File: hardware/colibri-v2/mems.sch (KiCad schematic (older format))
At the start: 9 parts

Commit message: Annotated Components
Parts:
- gave numbers to parts that had none: 9
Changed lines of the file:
@@
 $EndDescr
 $Comp
-L L3GD20 U?
+L L3GD20 U2
 U 1 1 55865E51
 P 4800 3350
-F 0 "U?" H 5200 3850 60  0000 C CNN
+F 0 "U2" H 5200 3850 60  0000 C CNN
 F 1 "L3GD20" H 4500 2850 60  0000 C CNN
 F 2 "" H 4800 3500 60  0000 C CNN
@@
 $EndComp
 $Comp
-L C C?
+L C C36
 U 1 1 55865EFE
 P 6100 3450
-F 0 "C?" H 6125 3550 50  0000 L CNN
+F 0 "C36" H 6125 3550 50  0000 L CNN
 F 1 "10nF/25V" H 6125 3350 50  0000 L CNN
 F 2 "" H 6138 3300 30  0000 C CNN
@@
 $EndComp
 $Comp
-L C C?
+L C C38
 U 1 1 55865F5E
 P 6750 3200
-F 0 "C?" H 6775 3300 50  0000 L CNN
+F 0 "C38" H 6775 3300 50  0000 L CNN
 F 1 "10nF" H 6775 3100 50  0000 L CNN
 F 2 "" H 6788 3050 30  0000 C CNN
@@
 $EndComp
 $Comp
-L C C?
+L C C40
 U 1 1 55865F9A
 P 7350 3200
-F 0 "C?" H 7375 3300 50  0000 L CNN
+F 0 "C40" H 7375 3300 50  0000 L CNN
 F 1 "10uF" H 7375 3100 50  0000 L CNN
 F 2 "" H 7388 3050 30  0000 C CNN
@@
 $EndComp
 $Comp
-L GND #PWR?
+L GND #PWR40
 U 1 1 55865FDB
 P 6750 3950
-F 0 "#PWR?" H 6750 3700 50  0001 C CNN
+F 0 "#PWR40" H 6750 3700 50  0001 C CNN
 F 1 "GND" H 6750 3800 50  0000 C CNN
 F 2 "" H 6750 3950 60  0000 C CNN
@@
 $EndComp
 $Comp
-L GND #PWR?
+L GND #PWR39
 U 1 1 558661BB
 P 3950 3950
-F 0 "#PWR?" H 3950 3700 50  0001 C CNN
+F 0 "#PWR39" H 3950 3700 50  0001 C CNN
 F 1 "GND" H 3950 3800 50  0000 C CNN
 F 2 "" H 3950 3950 60  0000 C CNN
@@
 MEMS_GYR_NCS
 $Comp
-L LSM303D U?
+L LSM303D U3
 U 1 1 55867183
 P 4800 5250
-F 0 "U?" H 5200 5750 60  0000 C CNN
+F 0 "U3" H 5200 5750 60  0000 C CNN
 F 1 "LSM303D" H 4550 4750 60  0000 C CNN
 F 2 "" H 4800 5400 60  0000 C CNN
@@
 MEMS_ACC_INT1
 $Comp
-L GND #PWR?
+L GND #PWR41
 U 1 1 5587241A
 P 6750 5950
-F 0 "#PWR?" H 6750 5700 50  0001 C CNN
+F 0 "#PWR41" H 6750 5700 50  0001 C CNN
 F 1 "GND" H 6750 5800 50  0000 C CNN
 F 2 "" H 6750 5950 60  0000 C CNN
@@
 $EndComp
 $Comp
-L C C?
+L C C37
 U 1 1 55872576
 P 6100 5350
-F 0 "C?" H 5950 5250 50  0000 L CNN
+F 0 "C37" H 5950 5250 50  0000 L CNN
 F 1 "4.7uF" H 5850 5450 50  0000 L CNN
 F 2 "" H 6138 5200 30  0000 C CNN
@@
 $EndComp
 $Comp
-L C C?
+L C C39
 U 1 1 55873CA6
 P 6750 5150
-F 0 "C?" H 6775 5250 50  0000 L CNN
+F 0 "C39" H 6775 5250 50  0000 L CNN
 F 1 "10nF" H 6775 5050 50  0000 L CNN
 F 2 "" H 6788 5000 30  0000 C CNN
@@
 $EndComp
 $Comp
-L C C?
+L C C41
 U 1 1 55873CAC
 P 7350 5150
-F 0 "C?" H 7375 5250 50  0000 L CNN
+F 0 "C41" H 7375 5250 50  0000 L CNN
 F 1 "10uF" H 7375 5050 50  0000 L CNN
 F 2 "" H 7388 5000 30  0000 C CNN
@@
 MEMS_ACC_NCS
 $Comp
-L C C?
+L C C35
 U 1 1 55878EB4
 P 3700 5500
-F 0 "C?" V 3750 5350 50  0000 L CNN
+F 0 "C35" V 3750 5350 50  0000 L CNN
 F 1 "0.22uF" V 3750 5600 50  0000 L CNN
 F 2 "" H 3738 5350 30  0000 C CNN
@@
 	1500 2300 8250 2300
 $Comp
-L PWR_FLAG #FLG?
+L PWR_FLAG #FLG1
 U 1 1 55FF3EA5
 P 1950 2100
-F 0 "#FLG?" H 1950 2195 50  0001 C CNN
+F 0 "#FLG1" H 1950 2195 50  0001 C CNN
 F 1 "PWR_FLAG" H 1950 2280 50  0000 C CNN
 F 2 "" H 1950 2100 60  0000 C CNN

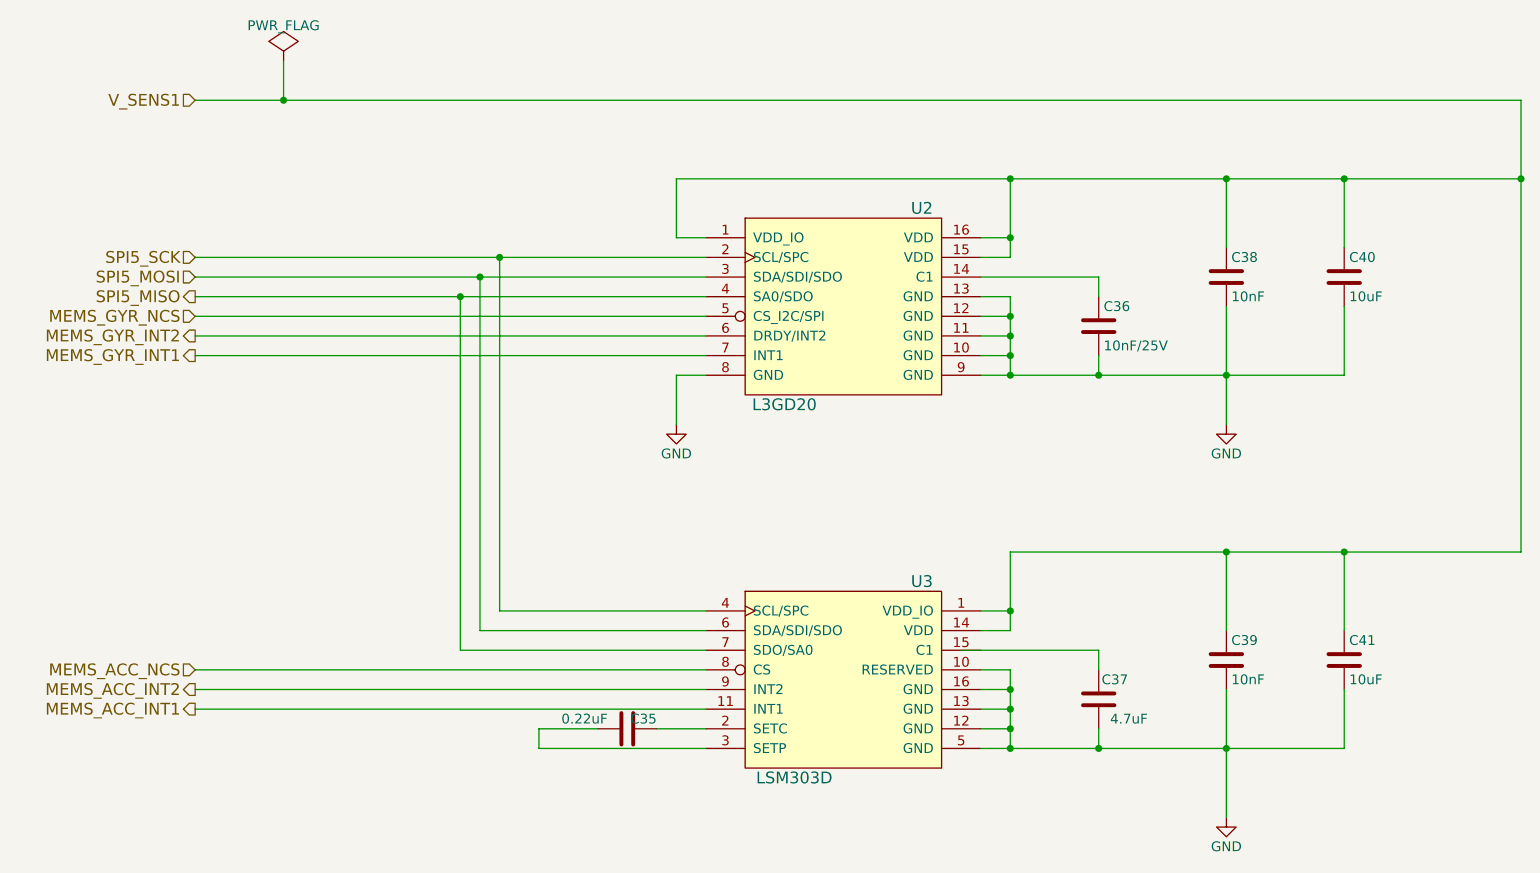
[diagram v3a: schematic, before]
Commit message: Separate VDD_IO
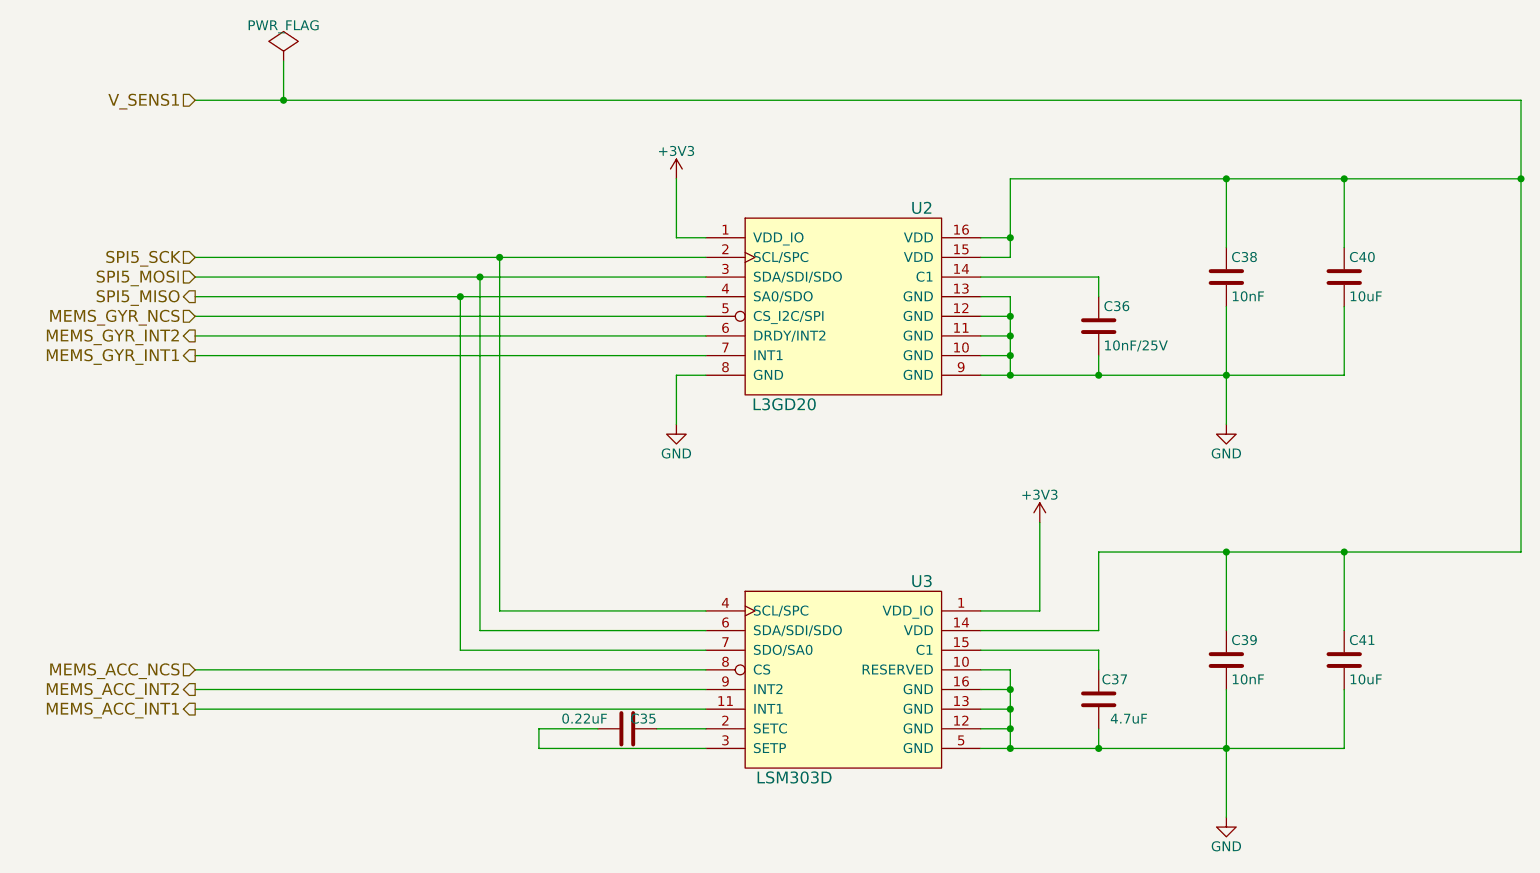
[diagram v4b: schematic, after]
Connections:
- net V_SENS1: no longer U2.1 (VDD_IO), U3.1 (VDD_IO)
- net at U3.15 (C1): now also C37.2
- new net +3V3: U2.1 (VDD_IO), U3.1 (VDD_IO)
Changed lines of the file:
@@
 	5650 2700 5650 3100
 Wire Wire Line
-	3950 2700 8250 2700
+	5650 2700 8250 2700
 Wire Wire Line
 	5650 3100 5500 3100
@@
 Wire Wire Line
 	3950 3000 4100 3000
-Connection ~ 5650 2700
 Wire Wire Line
 	3950 3950 3950 3700
@@
 Connection ~ 5650 5600
 Wire Wire Line
-	5400 5100 6100 5100
+	5500 5100 6100 5100
 Wire Wire Line
 	6100 5100 6100 5200
@@
 	6100 5600 6100 5500
 Wire Wire Line
-	5650 5000 5500 5000
-Connection ~ 5650 4900
+	6100 5000 5500 5000
 Wire Wire Line
 	7350 5600 7350 5300
@@
 Connection ~ 6750 5600
 Wire Wire Line
-	5650 4600 5650 5000
+	6100 4600 6100 5000
 Wire Wire Line
 	5650 5200 5650 5600
 Wire Wire Line
-	5650 4900 5500 4900
-Wire Wire Line
-	8250 4600 5650 4600
+	8250 4600 6100 4600
 Wire Wire Line
 	7350 4600 7350 5000
@@
 	1950 2100 1950 2300
 Connection ~ 1950 2300
+$Comp
+L +3V3 #PWR?
+U 1 1 5622ED95
+P 5800 4450
+F 0 "#PWR?" H 5800 4300 50  0001 C CNN
+F 1 "+3V3" H 5800 4590 50  0000 C CNN
+F 2 "" H 5800 4450 60  0000 C CNN
+F 3 "" H 5800 4450 60  0000 C CNN
+	1    5800 4450
+	1    0    0    -1
+$EndComp
+Wire Wire Line
+	5500 4900 5800 4900
+Wire Wire Line
+	5800 4900 5800 4450
+$Comp
+L +3V3 #PWR?
+U 1 1 5622EE37
+P 3950 2700
+F 0 "#PWR?" H 3950 2550 50  0001 C CNN
+F 1 "+3V3" H 3950 2840 50  0000 C CNN
+F 2 "" H 3950 2700 60  0000 C CNN
+F 3 "" H 3950 2700 60  0000 C CNN
+	1    3950 2700
+	1    0    0    -1
+$EndComp
 $EndSCHEMATC

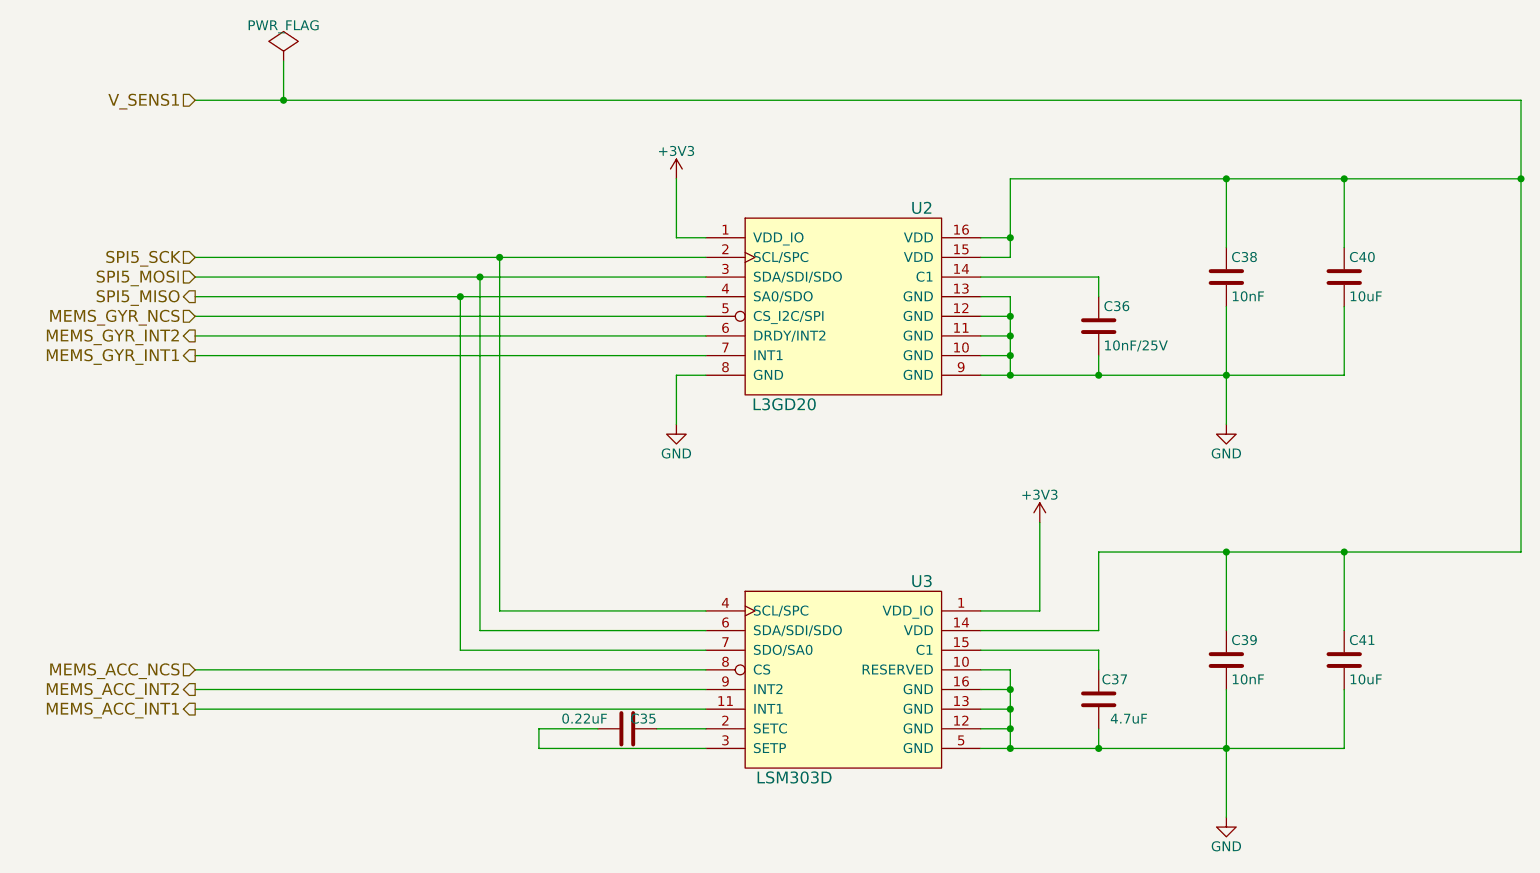
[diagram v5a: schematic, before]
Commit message: Reworked the buttons/leds sheet
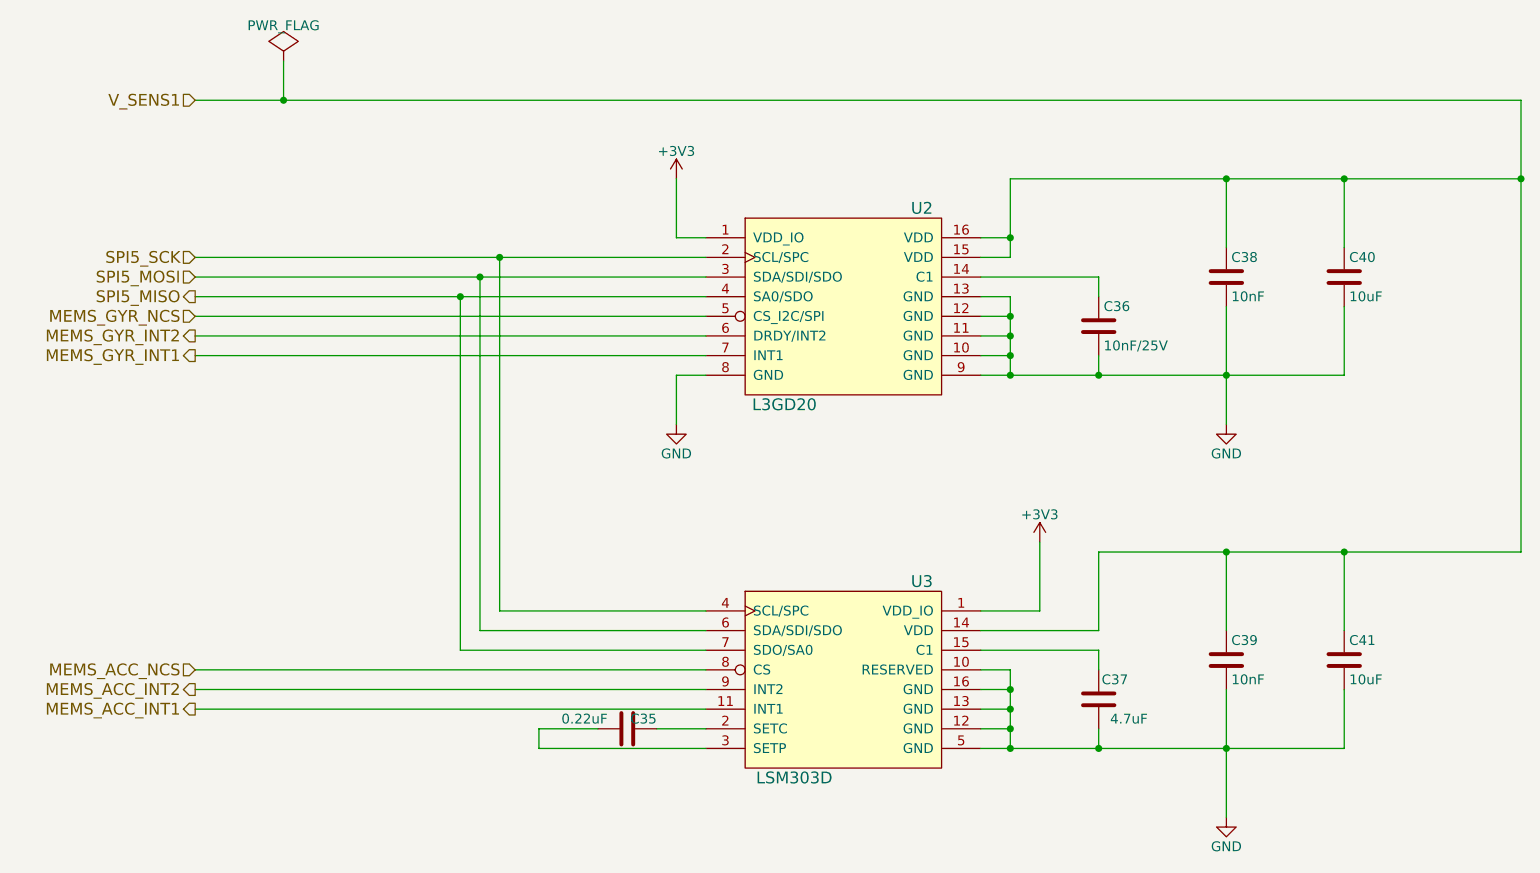
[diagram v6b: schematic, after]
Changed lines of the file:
@@
 $EndComp
 Wire Wire Line
-	5500 3700 7350 3700
+	5500 3700 5650 3700
+Wire Wire Line
+	5650 3700 6100 3700
+Wire Wire Line
+	6100 3700 6750 3700
+Wire Wire Line
+	6750 3700 7350 3700
 Wire Wire Line
 	7350 3700 7350 3350
 Wire Wire Line
-	6750 3350 6750 3950
+	6750 3350 6750 3700
+Wire Wire Line
+	6750 3700 6750 3950
 Connection ~ 6750 3700
 Wire Wire Line
@@
 	5500 3300 5650 3300
 Wire Wire Line
-	5650 3300 5650 3700
+	5650 3300 5650 3400
+Wire Wire Line
+	5650 3400 5650 3500
+Wire Wire Line
+	5650 3500 5650 3600
+Wire Wire Line
+	5650 3600 5650 3700
 Connection ~ 5650 3700
 Wire Wire Line
@@
 	5500 3000 5650 3000
 Wire Wire Line
-	5650 2700 5650 3100
-Wire Wire Line
-	5650 2700 8250 2700
+	5650 2700 5650 3000
+Wire Wire Line
+	5650 3000 5650 3100
+Wire Wire Line
+	5650 2700 6750 2700
+Wire Wire Line
+	6750 2700 7350 2700
+Wire Wire Line
+	7350 2700 8250 2700
 Wire Wire Line
 	5650 3100 5500 3100
@@
 	3950 3700 4100 3700
 Wire Wire Line
-	1500 3100 4100 3100
-Wire Wire Line
-	1500 3200 4100 3200
-Wire Wire Line
-	1500 3300 4100 3300
+	1500 3100 3050 3100
+Wire Wire Line
+	3050 3100 4100 3100
+Wire Wire Line
+	1500 3200 2950 3200
+Wire Wire Line
+	2950 3200 4100 3200
+Wire Wire Line
+	1500 3300 2850 3300
+Wire Wire Line
+	2850 3300 4100 3300
 Wire Wire Line
 	1500 3400 4100 3400
@@
 Connection ~ 5650 5500
 Wire Wire Line
-	5500 5600 7350 5600
+	5500 5600 5650 5600
+Wire Wire Line
+	5650 5600 6100 5600
+Wire Wire Line
+	6100 5600 6750 5600
+Wire Wire Line
+	6750 5600 7350 5600
 Connection ~ 5650 5600
 Wire Wire Line
@@
 Connection ~ 6100 5600
 Wire Wire Line
-	6750 5300 6750 5950
+	6750 5300 6750 5600
+Wire Wire Line
+	6750 5600 6750 5950
 Connection ~ 6750 5600
 Wire Wire Line
 	6100 4600 6100 5000
 Wire Wire Line
-	5650 5200 5650 5600
-Wire Wire Line
-	8250 4600 6100 4600
+	5650 5200 5650 5300
+Wire Wire Line
+	5650 5300 5650 5400
+Wire Wire Line
+	5650 5400 5650 5500
+Wire Wire Line
+	5650 5500 5650 5600
+Wire Wire Line
+	8250 4600 7350 4600
+Wire Wire Line
+	7350 4600 6750 4600
+Wire Wire Line
+	6750 4600 6100 4600
 Wire Wire Line
 	7350 4600 7350 5000
@@
 Connection ~ 6750 2700
 Wire Wire Line
-	8250 2300 8250 4600
+	8250 2300 8250 2700
+Wire Wire Line
+	8250 2700 8250 4600
 Connection ~ 7350 2700
 Connection ~ 7350 4600
@@
 V_SENS1
 Wire Wire Line
-	1500 2300 8250 2300
+	1500 2300 1950 2300
+Wire Wire Line
+	1950 2300 8250 2300
 $Comp
 L PWR_FLAG #FLG040
@@
 L +3V3 #PWR041
 U 1 1 5622ED95
-P 5800 4450
-F 0 "#PWR041" H 5800 4300 50  0001 C CNN
-F 1 "+3V3" H 5800 4590 50  0000 C CNN
-F 2 "" H 5800 4450 60  0000 C CNN
-F 3 "" H 5800 4450 60  0000 C CNN
-	1    5800 4450
+P 5800 4550
+F 0 "#PWR041" H 5800 4400 50  0001 C CNN
+F 1 "+3V3" H 5800 4690 50  0000 C CNN
+F 2 "" H 5800 4550 60  0000 C CNN
+F 3 "" H 5800 4550 60  0000 C CNN
+	1    5800 4550
 	1    0    0    -1
 $EndComp
@@
 	5500 4900 5800 4900
 Wire Wire Line
-	5800 4900 5800 4450
+	5800 4900 5800 4550
 $Comp
 L +3V3 #PWR042
